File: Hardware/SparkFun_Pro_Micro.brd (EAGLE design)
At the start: 17.8 x 33 mm, 33 parts, among them U2 MIC5219, U3 ATMEGA32U4, Y1 16MHz

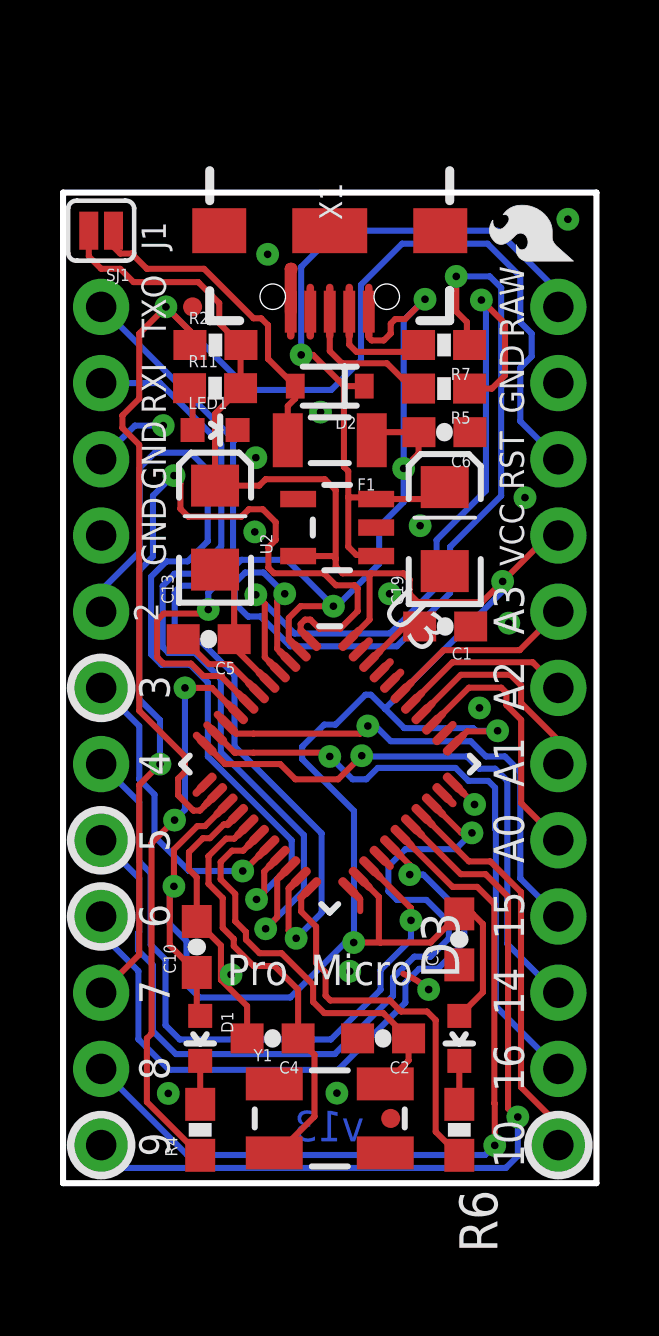
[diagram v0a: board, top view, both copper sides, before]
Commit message: Swap USB-B micro with USB-A male connector
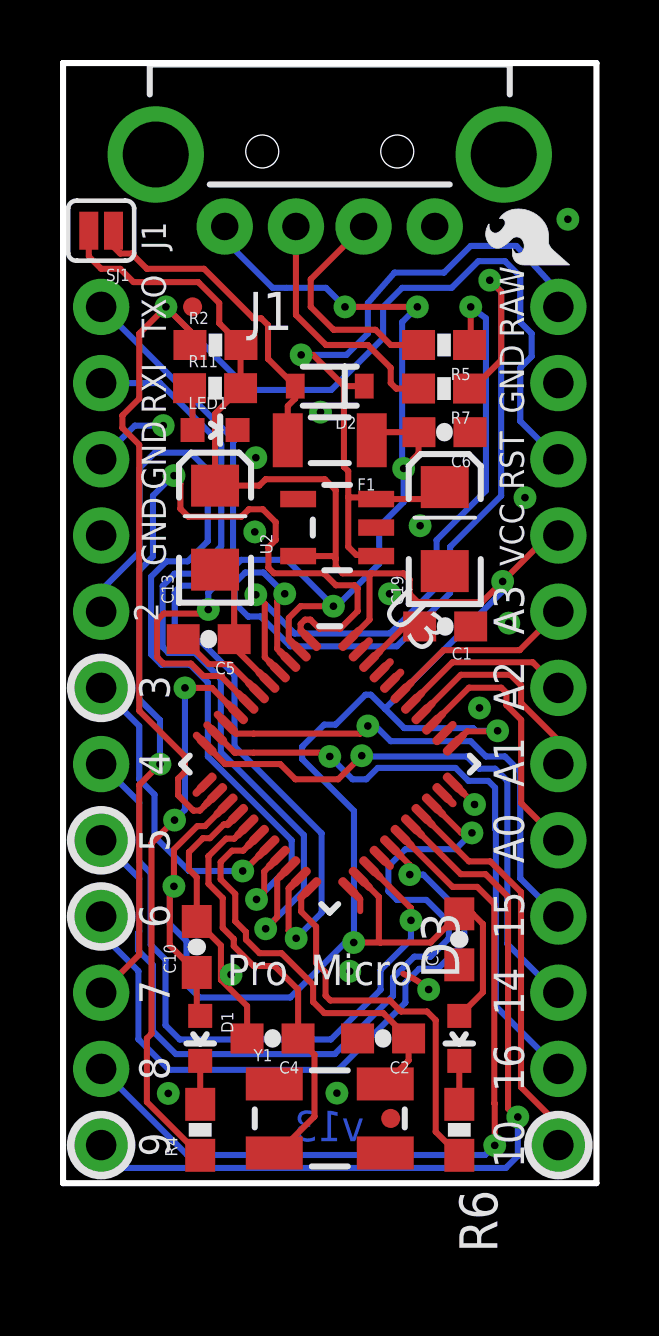
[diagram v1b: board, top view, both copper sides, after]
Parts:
- removed X1: (no value), Testing:USB-AB-MICRO-SMD-V03-IN&OUT
- added J1: USB-A-H, SparkFun-Connectors:USB-A-H
- moved R5 1.45 mm to (12.7, 27.9)
- moved R7 1.45 mm to (12.7, 26.5)
- moved U$1 0.18 mm to (16.9, 30.6)
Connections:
- removed net N$8: R5.2, X1.D+1
- new net N$9: J1.D+, R5.2
- net GND: now also J1.GND; no longer X1.GND1
- net N$6: now also J1.D-; no longer X1.D-1
- net UVCC: now also J1.VBUS; no longer X1.VBUS1
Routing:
- net N$9: track 0.00 -> 7.53 mm
- net N$8: track 4.79 -> 0.00 mm
- net N$6: track 3.62 -> 8.35 mm
- net UVCC: track 33.6 -> 37.5 mm, vias 4 -> 5
- net D+: track 24.6 -> 21.7 mm
- net RAW: track 25.8 -> 24.3 mm
- net GND: track 20.0 -> 18.5 mm, vias 17 -> 16
- net RESET: track 44.6 -> 43.2 mm
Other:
- board size 17.8 x 33 mm -> 17.8 x 37.3 mm

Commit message: Remove SparkFun logo on bottom silkscreen
This is cleverly hiding in the corner of the schematic as part of the title frame (look for "SFE" on the right).
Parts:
- removed U$11: LOGO-SFENEW, SparkFun:SFE-NEW-WEBLOGO
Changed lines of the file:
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@@
 <attribute name="VALUE" x="12.5476" y="4.0772" size="0.4064" layer="27" rot="R90"/>
 </element>
-<element name="U$11" library="SparkFun" package="SFE-NEW-WEBLOGO" value="LOGO-SFENEW" x="7.112" y="6.731" rot="MR90"/>
 <element name="U2" library="SparkFun" package="SOT23-5" value="MIC5219" x="9.13638125" y="21.8541625" smashed="yes" rot="R90">
 <attribute name="NAME" x="6.97738125" y="20.9651625" size="0.4064" layer="25" rot="R90"/>

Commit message: Add PartsNotIncluded logo to bottom silkscreen
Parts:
- added U$2: PNI-PRO-MICRO-SPLIT-LOGO-TEXT, PartsNotIncluded:PNI-PRO-MICRO-SPLIT-LOGO-TEXT
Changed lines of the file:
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@@
 <attribute name="PROD_ID" value="CONN-08367" x="8.89" y="34.29" size="1.778" layer="27" rot="R270" display="off"/>
 </element>
+<element name="U$2" library="PartsNotIncluded" package="PNI-PRO-MICRO-SPLIT-LOGO-TEXT" value="PNI-PRO-MICRO-SPLIT-LOGO-TEXT" x="8.26008125" y="6.6929" rot="MR90"/>
 </elements>
 <signals>
